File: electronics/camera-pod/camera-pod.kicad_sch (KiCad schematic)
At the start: 0 parts

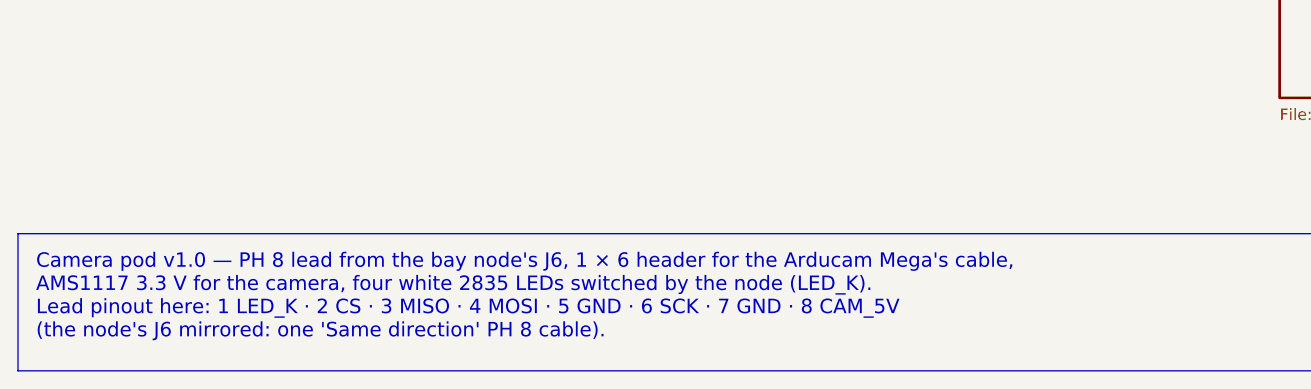
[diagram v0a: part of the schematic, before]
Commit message: Datasheet audit F1-F6: the pod's AP2114H, STB 5.1k, PC_DET hysteresis, the camera ESD's 100 nF, the eFuse step
The user approved the audit's fixes for the node, the hub and the pod
("Go pour 1"); docs/datasheet-audit.md marks F1-F6 applied.

* F1, camera pod: U1 AMS1117-3.3 -> AP2114H-3.3TRG1 (C150716, catalog
  ldo_1a, the node's U2).
  - The AMS1117 is specified stable only with 22 uF tantalum; the
    AP2114H is stable with the ceramic C2.
  - Same SOT-223 pinout, copper (the +3V3 pour and island round the
    tab stay) and 180 deg CPL correction.
  - One more extended type on the pod's Economic order: +$3.09 and
    $0.05 of parts (JLC_SINCE_QUOTE).
* F2, power hub: R214 (TJA1462 STB pull-down) 10k -> 5.1k (C23186,
  already on the board). With IO9 floating, STB's internal pull-up
  (20 kOhm minimum) left it at up to 1.10 V, over VIL 0.99 V.
* F3, bay node: R42 150k from MUX_SEL back to PC_DET, beside U7 (C22807,
  on the board since S1).
  - The laptop's VBUS rises at ~50 us/V through R11/R12, where the
    LVC1G32 wants <= 10 ns/V and warns of oscillation.
  - This gives ~0.14 V of hysteresis.
* F4, bay node: C28 100 nF (C14663) on U12/U13's VBUS pins (+3V3), above
  U12 by its pin 5. Between the two ICs their courtyards leave no room.
* F5, node and hub: firmware.md's first-flash procedure gains the
  irreversible DIS_USB_OTG_DOWNLOAD_MODE eFuse step. In USB-OTG
  download boot the ROM drives IO40 high: the node's DUT_FLT_N, the
  hub's PD_SCL. Nothing is burnt.
* F6, notes, hub:
  - the IMON filter is 0.9 ms, not 47 us: the pin is a current source;
  - the buck stops at ~3.8 V (internal UVLO);
  - SHDN turns on at >= 1 V;
  - the soft start stays under the limit only typically;
  - the CH224A note follows CH224 V2.1: the source PDOs are listed for
    both parts and readable under 100 W, which is still to check with
    ours (review R3); single-byte transfers; no "same die".
* F6, notes, node: TPS2553D; the LDO's 1.94 V x 0.4 A ~ 0.8 W; L1's
  7.5 A guarante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
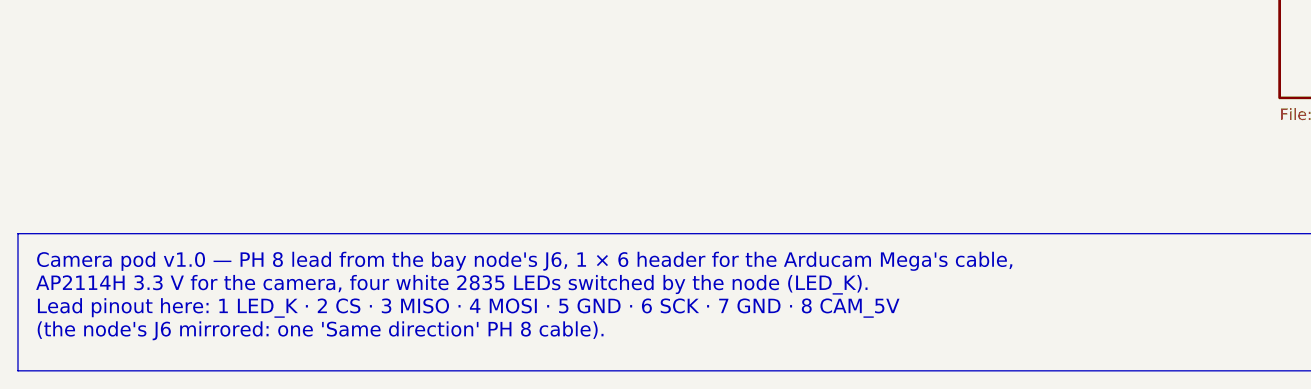
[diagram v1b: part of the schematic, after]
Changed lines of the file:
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@@
 		)
 	)
-	(text_box "Camera pod v1.0 — PH 8 lead from the bay node's J6, 1 × 6 header for the Arducam Mega's cable,\n  AMS1117 3.3 V for the camera, four white 2835 LEDs switched by the node (LED_K).\nLead pinout here: 1 LED_K · 2 CS · 3 MISO · 4 MOSI · 5 GND · 6 SCK · 7 GND · 8 CAM_5V\n  (the node's J6 mirrored: one 'Same direction' PH 8 cable)."
+	(text_box "Camera pod v1.0 — PH 8 lead from the bay node's J6, 1 × 6 header for the Arducam Mega's cable,\n  AP2114H 3.3 V for the camera, four white 2835 LEDs switched by the node (LED_K).\nLead pinout here: 1 LED_K · 2 CS · 3 MISO · 4 MOSI · 5 GND · 6 SCK · 7 GND · 8 CAM_5V\n  (the node's J6 mirrored: one 'Same direction' PH 8 cable)."
 		(exclude_from_sim no)
 		(at 30 115.57 0)
